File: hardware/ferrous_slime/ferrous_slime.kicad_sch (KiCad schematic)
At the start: 54 parts, among them J1 USB_C_Receptacle_USB2.0, Q1 DMG3415U, SW2 SW_SPDT, U1 SHTC3, U2 ICM-42670-P, U3 ESP32-C3-MINI-1, U4 TP4056, U5 M3406, Y1 32.768Hz

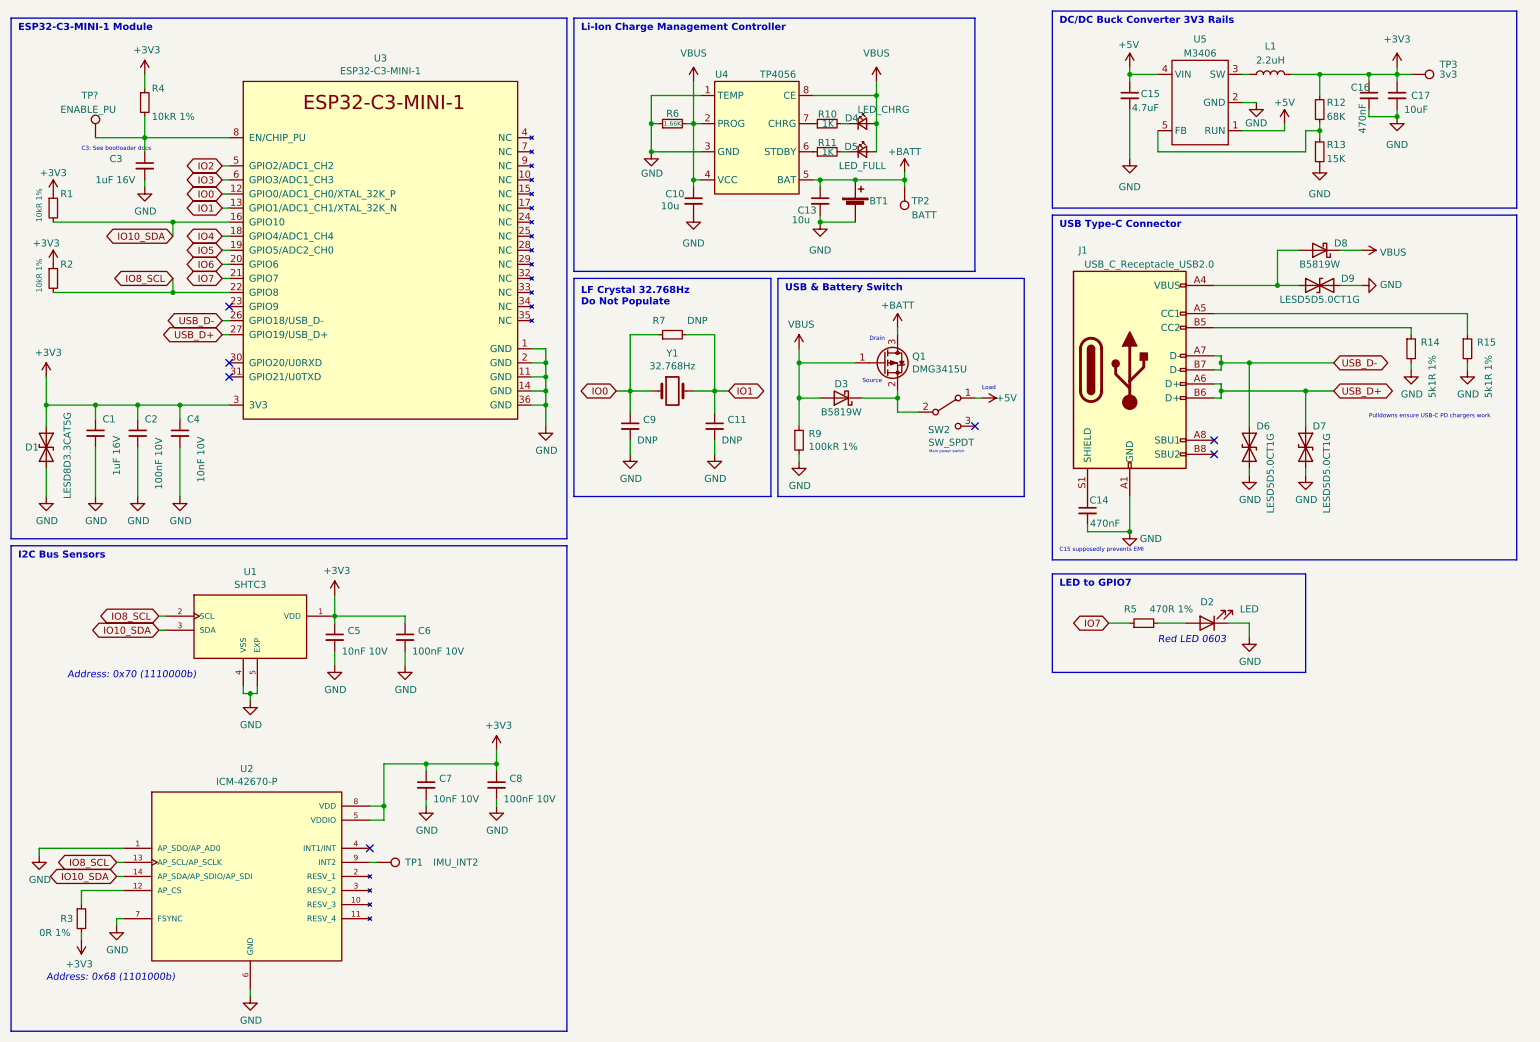
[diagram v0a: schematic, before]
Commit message: Added IMUs and resolved ERC
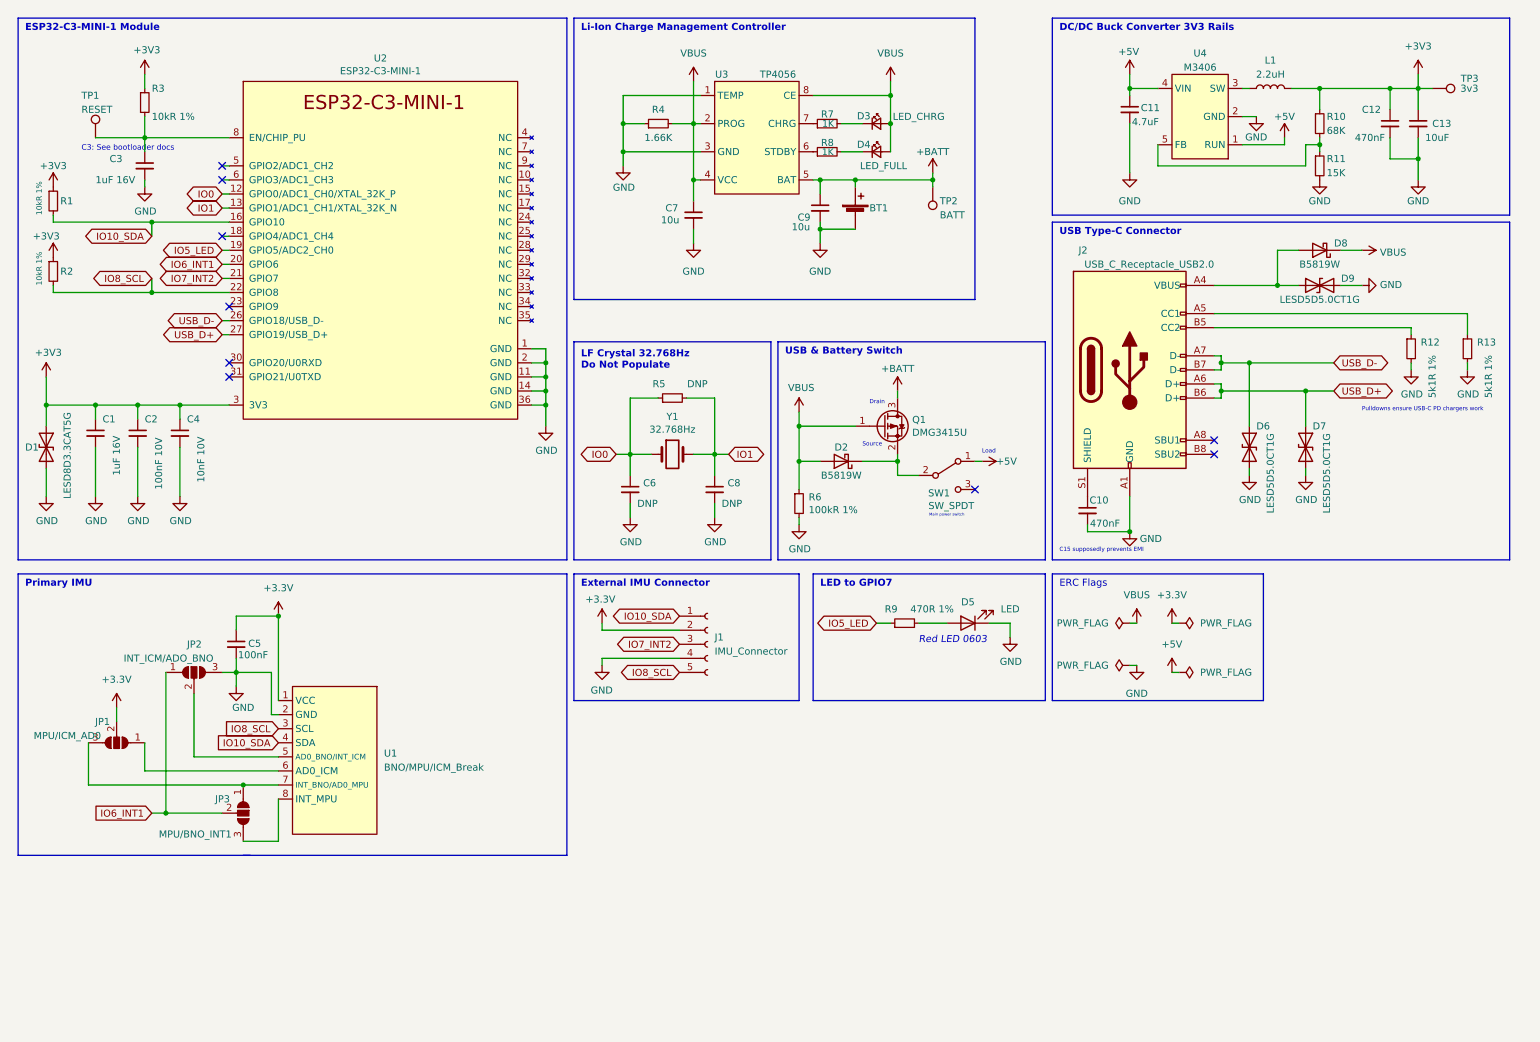
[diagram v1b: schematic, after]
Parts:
- removed C6, C8: 100nF 10V, Capacitor_SMD:C_0402_1005Metric, symbol Device:C_Small
- removed C7: 10nF 10V, Capacitor_SMD:C_0402_1005Metric, symbol Device:C_Small
- removed R3: 0R 1%, Resistor_SMD:R_0402_1005Metric, symbol Device:R_Small
- removed TP1: IMU_INT2, TestPoint:TestPoint_Pad_D1.0mm, symbol Connector:TestPoint
- removed U1: SHTC3, Rust_Board:SON100P200X200X80-5N, symbol Rust_Board:SHTC3
- removed U2: ICM-42670-P, Rust_Board:IC_ICM-42670-P, symbol Rust_Board:ICM-42670-P
- added J1: IMU_Connector, symbol Connector:Conn_01x05_Female
- added JP1: MPU/ICM_AD0, symbol Jumper:SolderJumper_3_Open
- added JP2: INT_ICM/ADO_BNO, symbol Jumper:SolderJumper_3_Open
- added JP3: MPU/BNO_INT1, symbol Jumper:SolderJumper_3_Open
- added U1: BNO/MPU/ICM_Break, symbol slimevr_pcb:BNO/MPU/ICM_Break
- C5: value 10nF 10V -> 100nF; footprint Capacitor_SMD:C_0402_1005Metric -> (none)
- TP1: renamed from TP?; value ENABLE_PU -> RESET
- renumbered C14 to C10, C15 to C11, C16 to C12, C17 to C13, C9 to C6, C10 to C7, C11 to C8, C13 to C9, D3 to D2, D4 to D3, D5 to D4, D2 to D5, J1 to J2, R12 to R10, R13 to R11, R14 to R12, R15 to R13, R4 to R3, R6 to R4, R7 to R5, R9 to R6, R10 to R7, R11 to R8, R5 to R9, SW2 to SW1, U3 to U2, U4 to U3, U5 to U4
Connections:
- net +3V3: now also J1.2 (Pin_2), JP1.2 (C), U1.1 (VCC)
- net GND: now also J1.4 (Pin_4), JP2.3 (B), U1.2 (GND)
- net IO10_SDA: now also J1.1 (Pin_1), U1.4 (SDA)
- net IO8_SCL: now also J1.5 (Pin_5), U1.3 (SCL)
- net IO2: no longer names the net of U2.5 (GPIO2/ADC1_CH2)
- net IO3: no longer names the net of U2.6 (GPIO3/ADC1_CH3)
- net IO4: no longer names the net of U2.18 (GPIO4/ADC1_CH4)
- net IO5 renamed IO5_LED
- net IO5_LED: now also R9.1
- net IO6 renamed IO6_INT1
- net IO6_INT1: now also JP2.1 (A), JP3.2 (C)
- net IO7 renamed IO7_INT2
- net IO7_INT2: now also J1.3 (Pin_3); no longer R9.1
- new net: JP2.2 (C), U1.5 (AD0_BNO/INT_ICM)
- new net: JP1.1 (A), U1.6 (AD0_ICM)
- new net: JP1.3 (B), JP3.1 (A), U1.7 (INT_BNO/AD0_MPU)
- new net: JP3.3 (B), U1.8 (INT_MPU)
- no-connect marks 7 -> 9
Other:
- note added: "ERC Flags"
- note added: "External IMU Connector"
- note added: "Primary IMU"
- note removed: "Address: 0x68 (1101000b)"
- note removed: "Address: 0x70 (1110000b)"
- note removed: "I2C Bus Sensors"
- moved on the sheet: BT1, C11, C12, C13, C6, C7, C8, C9, D2, D3, D4, D5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

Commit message: Plotted schematic
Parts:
- SW1: value SW_SPDT -> SW_PWR
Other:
- note added: "C10 supposedly prevents EMI"
- note removed: "C15 supposedly prevents EMI"
- note removed: "Main power switch"
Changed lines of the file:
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@@
   )
   (text "ERC Flags\n" (at 201.93 116.84 0)
-    (effects (font (size 1.27 1.27)) (justify left bottom))
+    (effects (font (size 1.27 1.27) (thickness 0.254) bold) (justify left bottom))
   )
   (text "LF Crystal 32.768Hz \nDo Not Populate" (at 115.57 77.47 0)
@@
     (effects (font (size 1.27 1.27) (thickness 0.254) bold) (justify left bottom))
   )
-  (text "C15 supposedly prevents EMI" (at 201.93 110.49 0)
+  (text "C10 supposedly prevents EMI" (at 201.93 110.49 0)
     (effects (font (size 0.75 0.75)) (justify left bottom))
-  )
-  (text "Main power switch" (at 178.4091 104.0683 0)
-    (effects (font (size 0.5 0.5)) (justify left bottom))
   )
   (text "LED to GPIO7" (at 158.75 116.84 0)
@@
     (in_bom yes) (on_board yes)
     (property "Reference" "SW1" (id 0) (at 180.2061 99.7149 0))
-    (property "Value" "SW_SPDT" (id 1) (at 182.4142 101.9991 0))
+    (property "Value" "SW_PWR" (id 1) (at 182.4142 101.9991 0))
     (property "Footprint" "" (id 2) (at 181.61 96.52 0)
       (effects (font (size 1.27 1.27)) hide)
@@
     )
     (path "/aa72736b-e9e9-48e9-967e-85bff4559e21"
-      (reference "SW1") (unit 1) (value "SW_SPDT") (footprint "")
+      (reference "SW1") (unit 1) (value "SW_PWR") (footprint "")
     )
     (path "/d0af8d88-ce7c-4eb5-8b78-ccc3644aafcf"

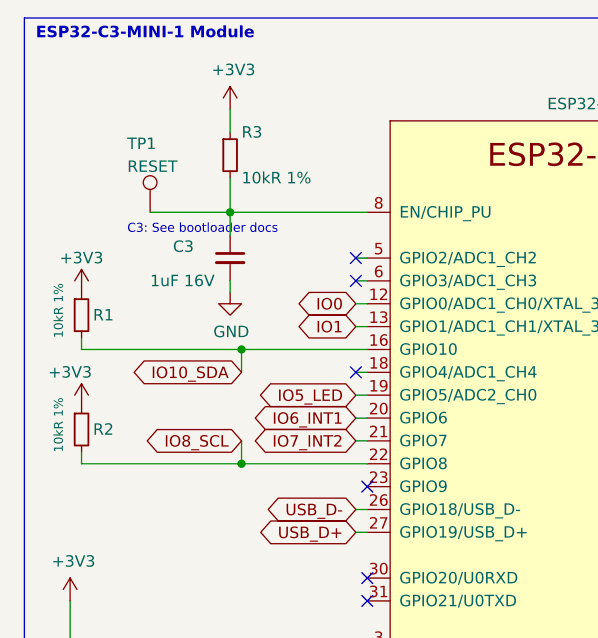
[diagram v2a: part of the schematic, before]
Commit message: Removed I2C pullups since they are already in breakouts
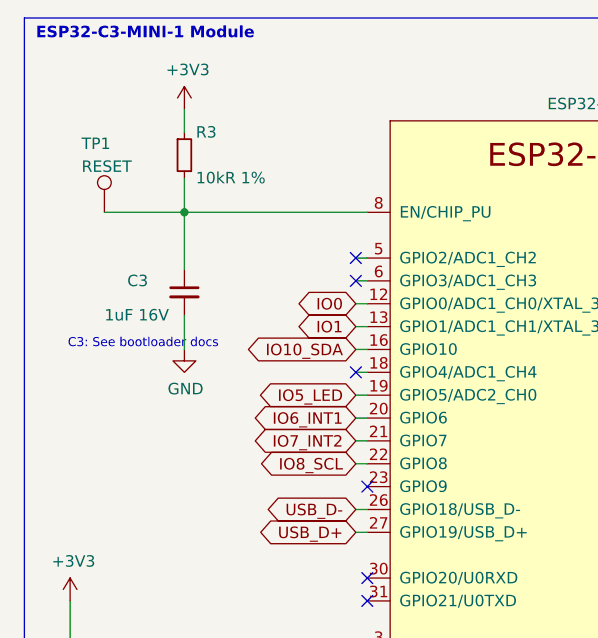
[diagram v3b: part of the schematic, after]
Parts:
- removed R1, R2: 10kR 1%, Resistor_SMD:R_0402_1005Metric, symbol Device:R_Small
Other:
- moved on the sheet: C3, R3, TP1

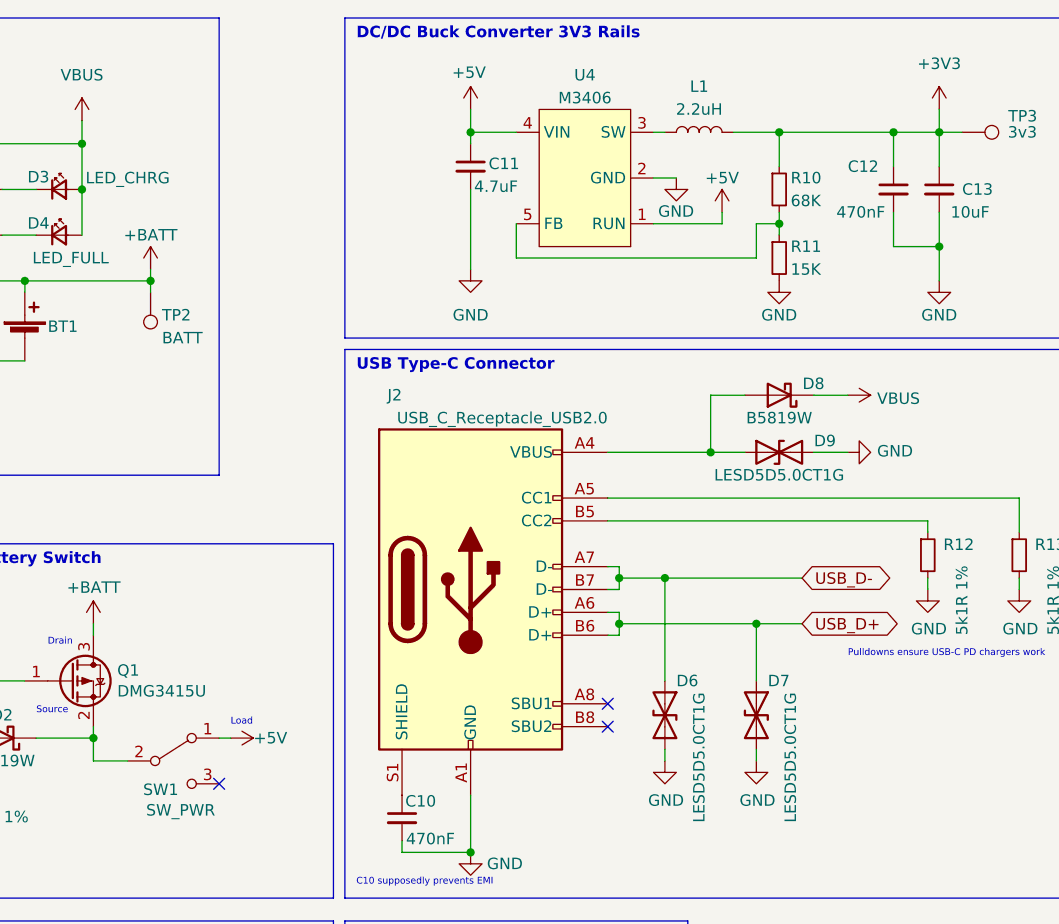
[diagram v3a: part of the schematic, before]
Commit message: Assigned most footprints
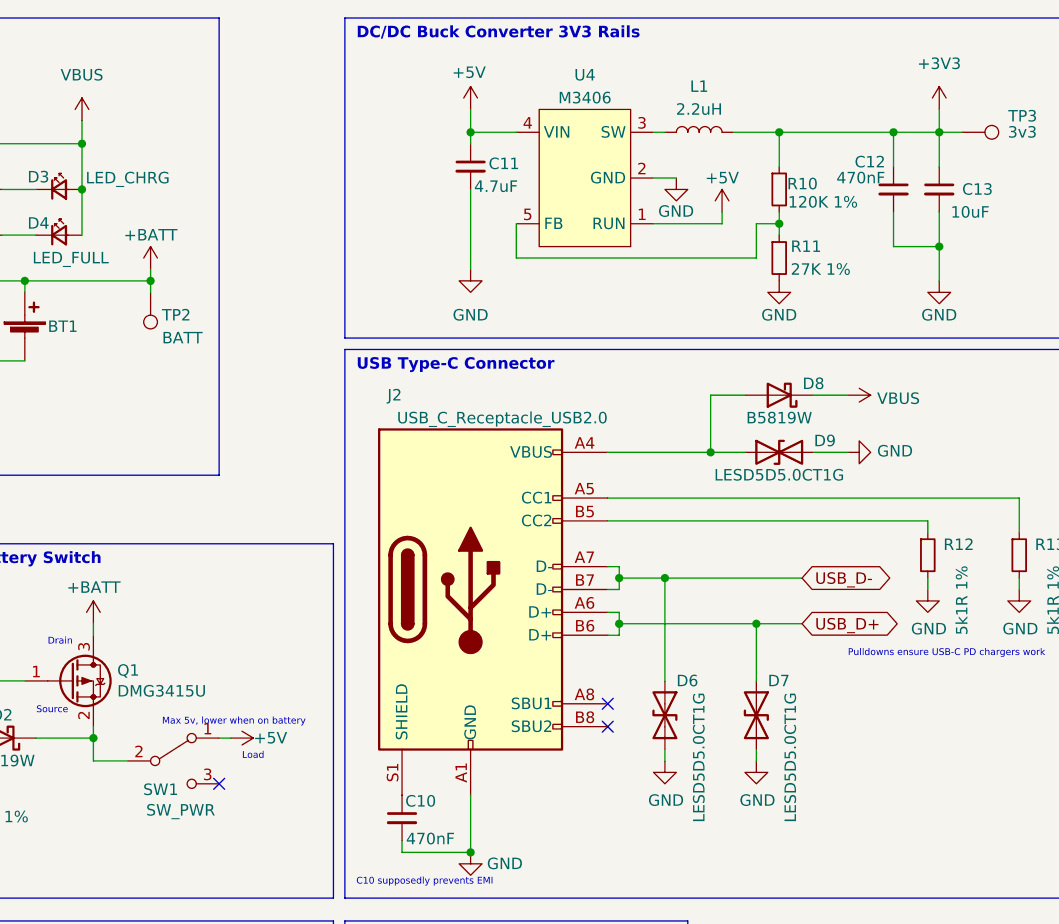
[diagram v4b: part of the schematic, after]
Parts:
- BT1: footprint (none) -> Connector_JST:JST_PH_S2B-PH-K_1x02_P2.00mm_Horizontal
- C1, C2, C3, C4, C6, C8: footprint Capacitor_SMD:C_0402_1005Metric -> Capacitor_SMD:C_0603_1608Metric
- C10, C11, C12, C13, C5, C7, C9: footprint (none) -> Capacitor_SMD:C_0603_1608Metric
- D3, D4: footprint (none) -> LED_SMD:LED_0603_1608Metric
- J1: footprint (none) -> Connector_JST:JST_PH_S5B-PH-K_1x05_P2.00mm_Horizontal
- JP1, JP2, JP3: footprint (none) -> Jumper:SolderJumper-3_P1.3mm_Open_Pad1.0x1.5mm
- R10: value 68K -> 120K 1%; footprint (none) -> Resistor_SMD:R_0603_1608Metric
- R11: value 15K -> 27K 1%; footprint (none) -> Resistor_SMD:R_0603_1608Metric
- R12, R13, R3, R5, R6, R9: footprint Resistor_SMD:R_0402_1005Metric -> Resistor_SMD:R_0603_1608Metric
- R4, R7, R8: footprint (none) -> Resistor_SMD:R_0603_1608Metric
- SW1: footprint (none) -> Button_Switch_THT:SW_CuK_OS102011MA1QN1_SPDT_Angled
- TP1, TP2, TP3: footprint (none) -> TestPoint:TestPoint_Pad_D1.0mm
- U1: footprint (none) -> slimevr_pcb:BNO_MPU_Breakout
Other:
- note added: "Max 5v, lower when on battery"

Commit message: Assigned remaining footprints, did layout
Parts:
- removed BT1: Battery_Cell, Connector_JST:JST_PH_S2B-PH-K_1x02_P2.00mm_Horizontal, symbol Device:Battery_Cell
- added J2: Battery_Connector, Connector_JST:JST_PH_S2B-PH-K_1x02_P2.00mm_Horizontal, symbol Connector:Conn_01x02_Female
- D1: footprint Rust_Board:SOD-882 -> Diode_SMD:D_SOD-323_HandSoldering
- L1: footprint (none) -> Inductor_SMD:L_7.3x7.3_H4.5
- U1: footprint slimevr_pcb:BNO_MPU_Breakout -> slimevr_pcb:BNO_MPU_ICM_Breakout
- U3: footprint slimevr_pcb:TP4056 -> Package_SO:HTSOP-8-1EP_3.9x4.9mm_P1.27mm_EP2.4x3.2mm
- renumbered C3 to C2, C2 to C3, J2 to J3, R3 to R1, R12 to R10, R13 to R11, R4 to R2, R5 to R3, R6 to R4, R7 to R5, R8 to R6, R9 to R7, R10 to R8, R11 to R9
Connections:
- net +BATT: now also J2.2 (Pin_2)
- net GND: now also J2.1 (Pin_1)

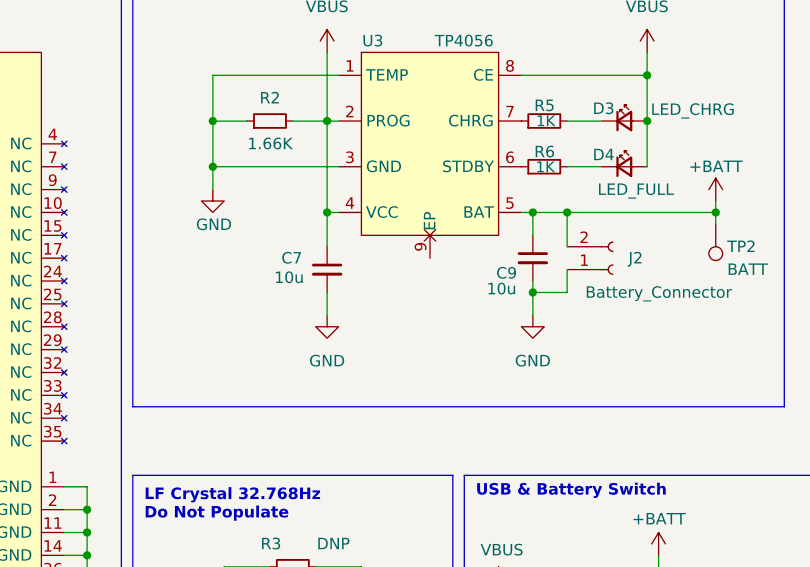
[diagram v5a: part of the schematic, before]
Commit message: Routed all nets, fixed most of silkscreen
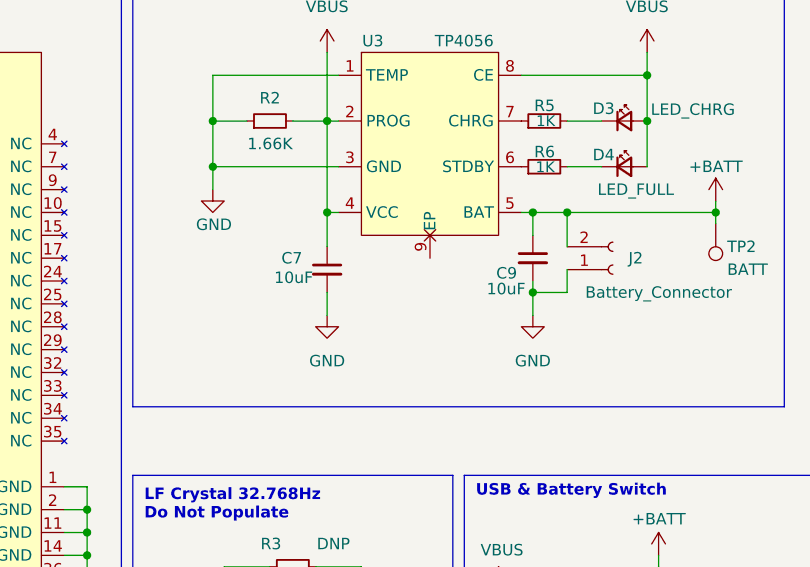
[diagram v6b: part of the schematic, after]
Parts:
- C7, C9: value 10u -> 10uF
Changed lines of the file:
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@@
       (effects (font (size 1.27 1.27)) (justify left))
     )
-    (property "Value" "10u" (id 1) (at 130.0118 50.4264 0)
+    (property "Value" "10uF" (id 1) (at 130.0118 50.4264 0)
       (effects (font (size 1.27 1.27)) (justify left))
     )
@@
       (effects (font (size 1.27 1.27)) (justify left))
     )
-    (property "Value" "10u" (id 1) (at 153.6126 51.6806 0)
+    (property "Value" "10uF" (id 1) (at 153.6126 51.6806 0)
       (effects (font (size 1.27 1.27)) (justify left))
     )
@@
     )
     (path "/08cfdadd-3136-4a95-9851-cb9ac660ddb9"
-      (reference "C7") (unit 1) (value "10u") (footprint "Capacitor_SMD:C_0603_1608Metric")
+      (reference "C7") (unit 1) (value "10uF") (footprint "Capacitor_SMD:C_0603_1608Metric")
     )
     (path "/00000000-0000-0000-0000-0000623813bf"
@@
     )
     (path "/f45f95a2-60b3-44cc-9210-f82745a046c6"
-      (reference "C9") (unit 1) (value "10u") (footprint "Capacitor_SMD:C_0603_1608Metric")
+      (reference "C9") (unit 1) (value "10uF") (footprint "Capacitor_SMD:C_0603_1608Metric")
     )
     (path "/15ebd1cd-0903-439e-92b7-4f09b8973a3b"
